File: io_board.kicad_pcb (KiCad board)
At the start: 2 copper layers, 100 x 100 mm, 85 parts, among them J1 TBP02R1-381-04, J10 TBP02R1-381-02, J11 TBP02R1-381-02, J12 TBP02R1-381-04, J13 CI1103M1VR0, J15 TBP02R1-381-02, J2 25SH-B-03-TR, J3 TBP02R1-381-02, J4 TBP02R1-381-02, J5 TBP02R1-381-02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

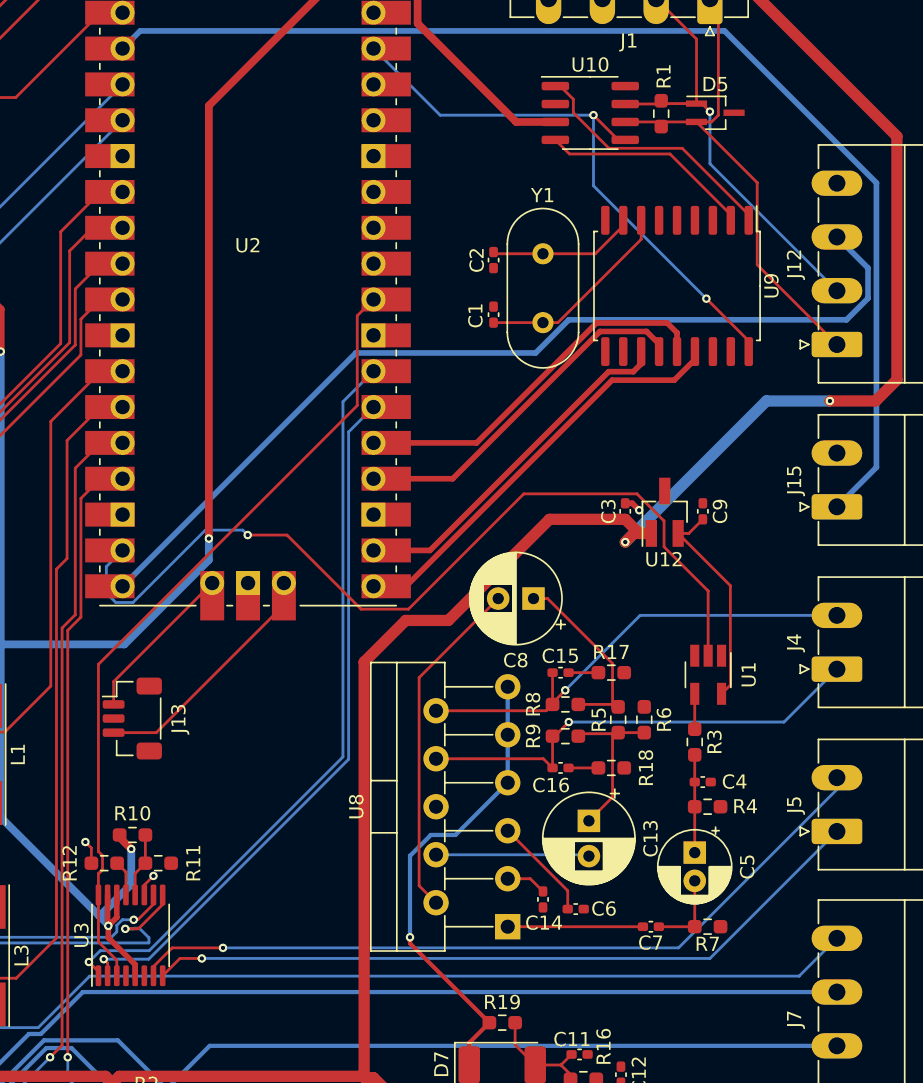
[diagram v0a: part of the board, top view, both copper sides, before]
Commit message: removed the mcp2515 can controller because I can use the can2040 library instead
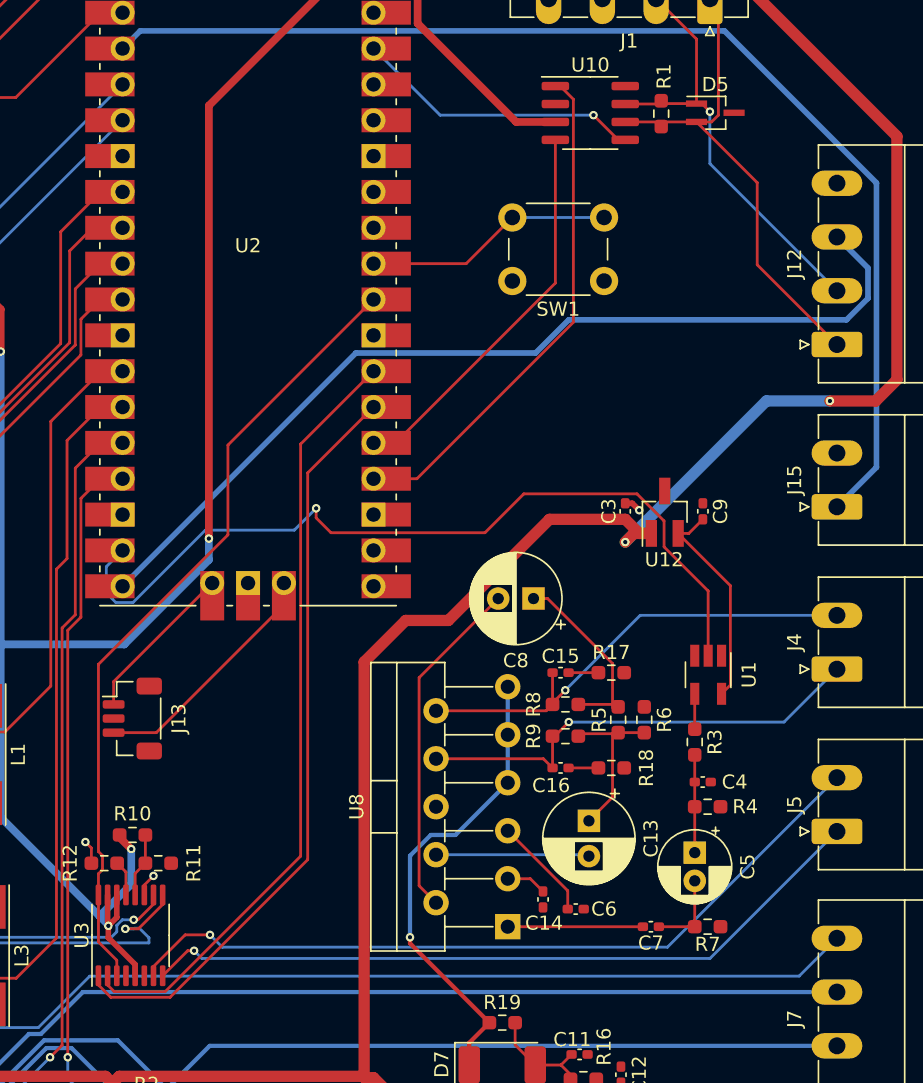
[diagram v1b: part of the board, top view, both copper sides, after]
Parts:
- removed C1, C2: 15pF, Capacitor_SMD:C_0402_1005Metric_Pad0.74x0.62mm_HandSolder
- removed U9: MCP2515-xSO, Package_SO:SOIC-18W_7.5x11.6mm_P1.27mm
- removed Y1: 16MHz, Crystal:Crystal_HC49-U_Vertical
- added SW1: SW_Push, Button_Switch_THT:SW_PUSH_6mm, F.Cu at (125.0, 78.5)
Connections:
- U10 pad 1: /Communication/CAN_TX -> /CAN_TX
- U10 pad 4: /Communication/CAN_RX -> /CAN_RX
- U2 pad 21: /CAN_MISO -> unconnected-(U2-GPIO16-Pad21)
- U2 pad 22: /CAN_INT -> unconnected-(U2-GPIO17-Pad22)
- U2 pad 24: /CAN_SCK -> /CAN_TX
- U2 pad 25: /CAN_MOSI -> /CAN_RX
- U2 pad 26: /DOOR_ENB -> /DOOR_ENA
- U2 pad 27: /DOOR_ENA -> /DOOR_ENB
- U2 pad 30: unconnected-(U2-RUN-Pad30) -> /RESET
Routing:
- net /CAN_TX: track 0.00 -> 36.2 mm
- net /CAN_MISO: track 30.0 -> 0.00 mm
- net /CAN_RX: track 0.00 -> 27.7 mm
- net /CAN_MOSI: track 26.6 -> 0.00 mm
- net /CAN_SCK: track 25.5 -> 0.00 mm
- net /CAN_INT: track 25.3 -> 0.00 mm
- net 3V3: track 41.8 -> 20.5 mm, vias 2 -> 1
- net /Communication/CAN_TX: track 18.4 -> 0.00 mm
- net /RESET: track 0.00 -> 17.7 mm
- net /Communication/CAN_RX: track 15.0 -> 0.00 mm
- net Net-(U9-OSC2): track 14.3 -> 0.00 mm
- net Net-(U9-OSC1): track 10.5 -> 0.00 mm
- net /DOOR_ENB: track 50.2 -> 55.0 mm, vias 1 -> 0
- net /AUDIO_PWM: track 62.8 -> 59.9 mm
- net /DOOR_ENA: track 53.5 -> 53.9 mm, vias 1 -> 0
